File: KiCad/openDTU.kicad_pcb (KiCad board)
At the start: 2 copper layers, 42 x 46.7 mm, 26 parts, among them J1 USB_C_Receptacle_USB2.0, J2 Conn_Coaxial, U3 ESP32-WROOM-32, U4 nRF24L01P, U5 NCP1117-3.3_SOT223, Y1 Crystal

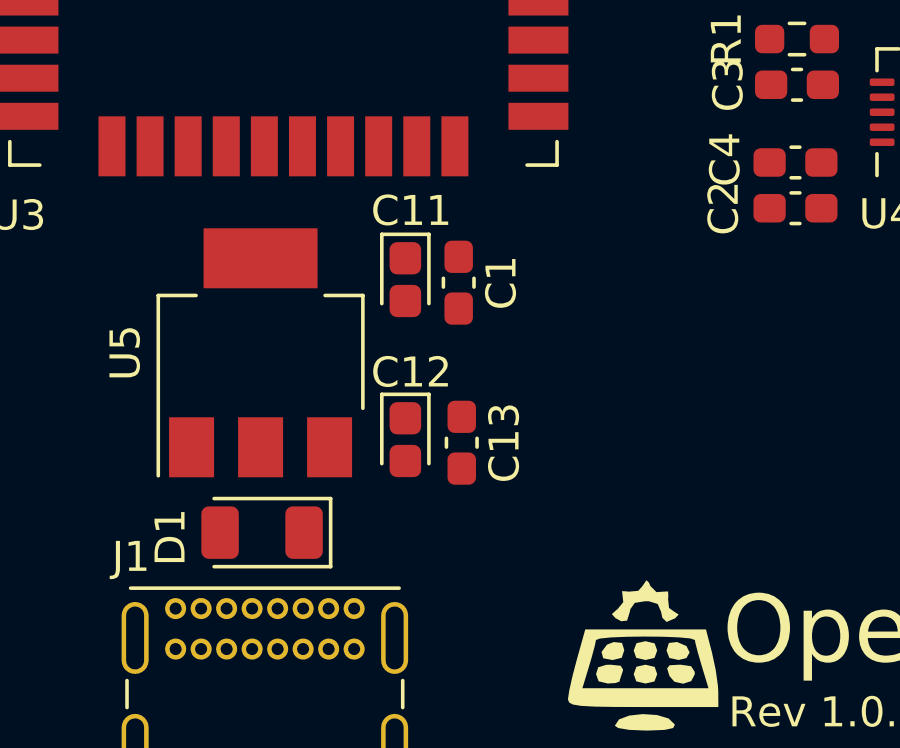
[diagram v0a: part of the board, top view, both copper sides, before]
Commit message: adding 3D Model for USB-C connector
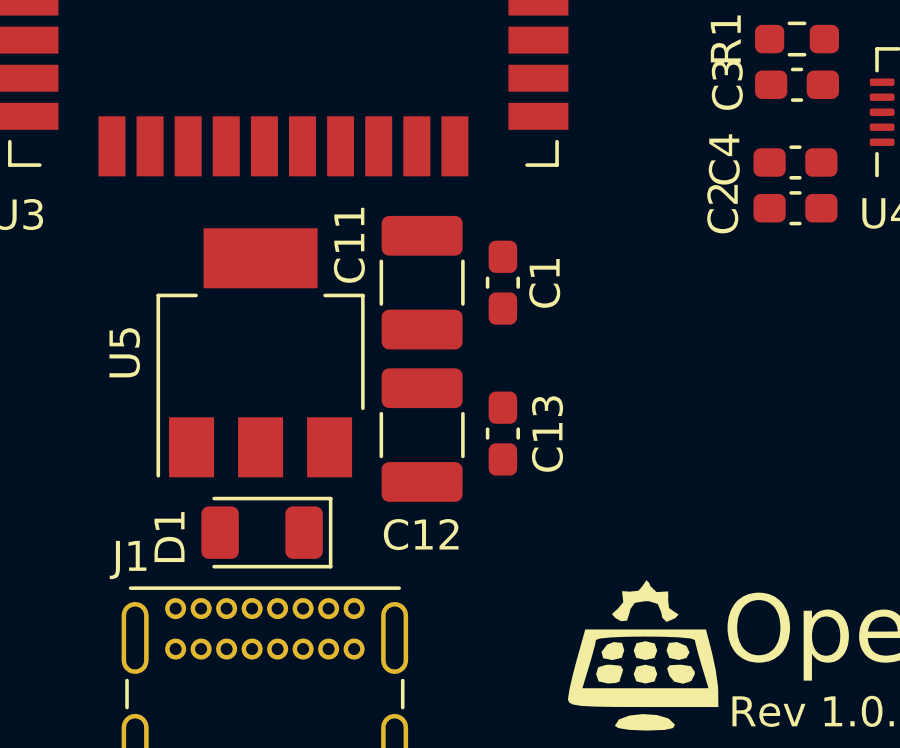
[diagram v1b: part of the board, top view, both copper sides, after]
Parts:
- C11, C12: footprint Capacitor_Tantalum_SMD:CP_EIA-1608-10_AVX-L -> Capacitor_SMD:C_1210_3225Metric_Pad1.33x2.70mm_HandSolder
- moved C1 1.47 mm to (143.5, 100.2)
- moved C13 1.41 mm to (143.5, 105.2), turned to 90 degrees
- moved C12 0.58 mm to (140.8, 105.3), turned to 90 degrees
- moved C11 0.57 mm to (140.8, 100.2)

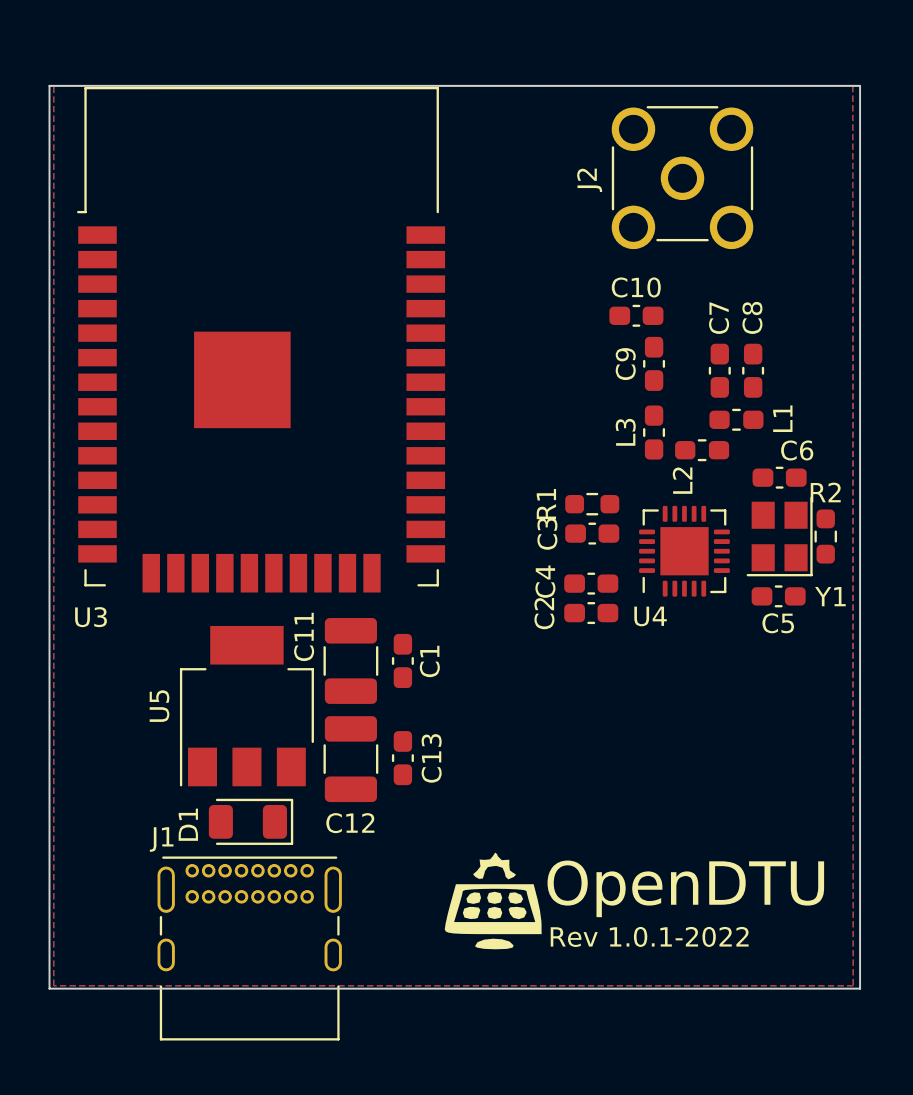
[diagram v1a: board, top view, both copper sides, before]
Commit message: adding microSD socket and reset switch to schematic
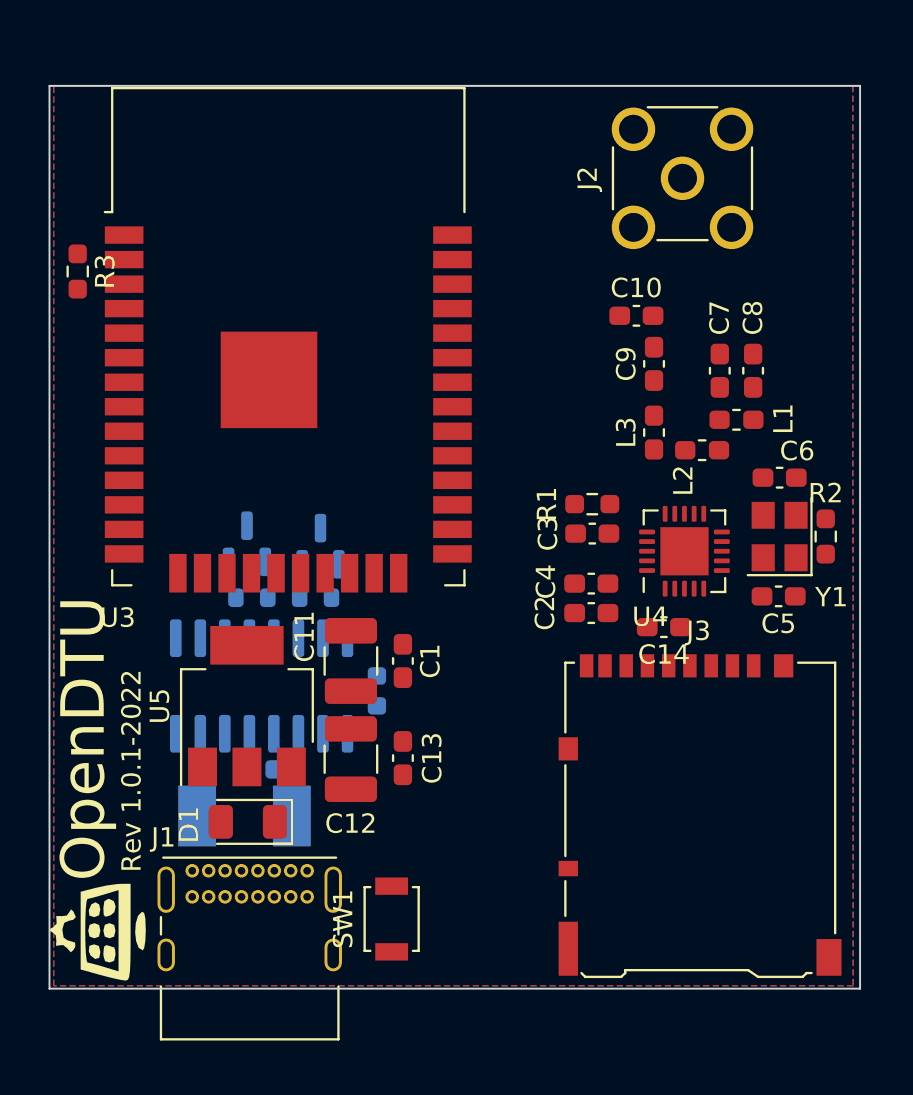
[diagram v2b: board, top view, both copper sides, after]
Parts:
- added C14: 100nF, Capacitor_SMD:C_0603_1608Metric_Pad1.08x0.95mm_HandSolder, F.Cu at (157.0, 98.4)
- added C15: 100n, Capacitor_SMD:C_0603_1608Metric, B.Cu at (136.0, 105.8)
- added C16: 100n, Capacitor_SMD:C_0603_1608Metric, B.Cu at (142.1, 101.7)
- added F1: F5, Fuse:Fuse_Littelfuse-NANO2-451_453, B.Cu at (135.3, 108.2)
- added J3: Micro_SD_Card, Connector_Card:microSD_HC_Hirose_DM3AT-SF-PEJM5, F.Cu at (158.8, 108.2)
- added Q1: BC817, Package_TO_SOT_SMD:SOT-23, B.Cu at (135.4, 94.1)
- added Q2: BC817, Package_TO_SOT_SMD:SOT-23, B.Cu at (139.2, 94.2)
- added R3: 10k, Resistor_SMD:R_0603_1608Metric_Pad0.98x0.95mm_HandSolder, F.Cu at (126.6, 80.0)
- added R4: 10k, Resistor_SMD:R_0603_1608Metric, B.Cu at (135.6, 96.9)
- added R5: 10k, Resistor_SMD:R_0603_1608Metric, B.Cu at (138.9, 96.9)
- added SW1: SW_Push, Button_Switch_SMD:SW_SPST_B3U-1000P, F.Cu at (142.9, 113.5)
- added U1: CH340C, Package_SO:SOIC-16_3.9x9.9mm_P1.27mm, B.Cu at (136.1, 101.5)
- moved G*** 20.6 mm to (127.6, 114.2), turned to 90 degrees
- moved U3 1.38 mm to (137.5, 86.4)
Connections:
- J1 pad A4: VBUS -> Net-(J1-PadA4)
- J1 pad A6: unconnected-(J1-PadA6) -> Net-(J1-PadA6)
- J1 pad A7: unconnected-(J1-PadA7) -> Net-(J1-PadA7)
- J1 pad A9: VBUS -> Net-(J1-PadA4)
- J1 pad B4: VBUS -> Net-(J1-PadA4)
- J1 pad B6: unconnected-(J1-PadB6) -> (no net)
- J1 pad B7: unconnected-(J1-PadB7) -> (no net)
- J1 pad B9: VBUS -> Net-(J1-PadA4)
- U3 pad 3: unconnected-(U3-Pad3) -> /ESP_EN

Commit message: adding BOOT switch buttom
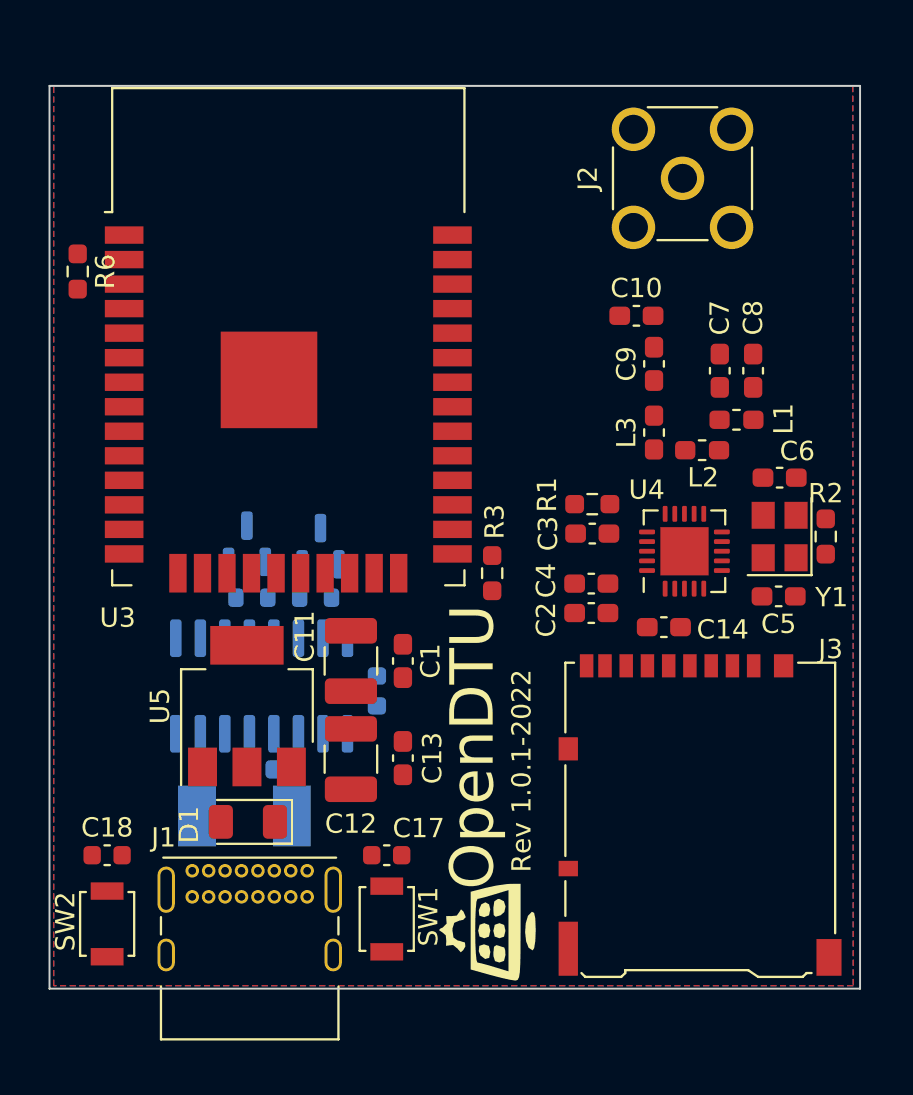
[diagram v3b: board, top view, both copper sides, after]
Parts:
- added C17: 1µ, Capacitor_SMD:C_0603_1608Metric, F.Cu at (142.6, 110.2)
- added C18: 1µ, Capacitor_SMD:C_0603_1608Metric, F.Cu at (128.1, 110.2)
- added R6: 10k, Resistor_SMD:R_0603_1608Metric_Pad0.98x0.95mm_HandSolder, F.Cu at (126.6, 80.0)
- added SW2: SW_Push, Button_Switch_SMD:SW_SPST_B3U-1000P, F.Cu at (128.1, 113.8)
- moved R3 26.5 mm to (148.1, 95.6), turned to 90 degrees
- moved G*** 20.2 mm to (147.8, 114.2)
- moved SW1 0.25 mm to (142.6, 113.5)
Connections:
- Q2 pad 3: /ESP_IO0/ETH_REFCLK -> /ESP.IO0
- R3 pad 2: /ESP_EN -> /ESP.IO0
- SW1 pad 2: /ESP_EN -> /ESP.IO0
- U1 pad 2: /ESP_RXD/BTN2 -> /ESP.RXD
- U1 pad 3: /ESP_TXD/BTN1 -> /ESP.TXD
- U3 pad 25: unconnected-(U3-Pad25) -> /ESP.IO0
- U3 pad 34: unconnected-(U3-Pad34) -> /ESP.RXD
- U3 pad 35: unconnected-(U3-Pad35) -> /ESP.TXD

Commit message: adding User (GPIO1) and Power LED
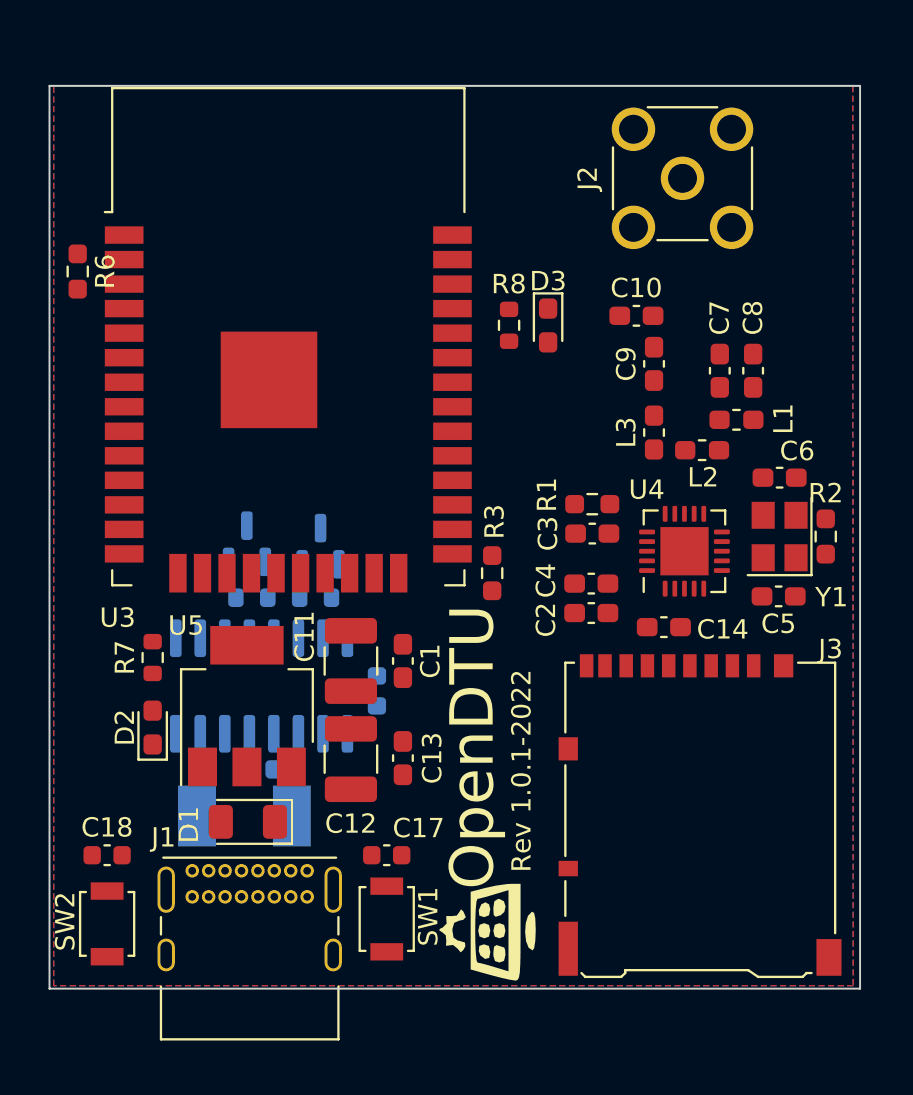
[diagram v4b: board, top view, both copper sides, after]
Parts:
- added D2: LED, LED_SMD:LED_0603_1608Metric_Pad1.05x0.95mm_HandSolder, F.Cu at (130.5, 103.6)
- added D3: LED, LED_SMD:LED_0603_1608Metric_Pad1.05x0.95mm_HandSolder, F.Cu at (151.0, 82.8)
- added R7: 10k, Resistor_SMD:R_0603_1608Metric, F.Cu at (130.5, 100.0)
- added R8: 10k, Resistor_SMD:R_0603_1608Metric, F.Cu at (149.0, 82.8)

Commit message: reduce the board size and beautify the placement
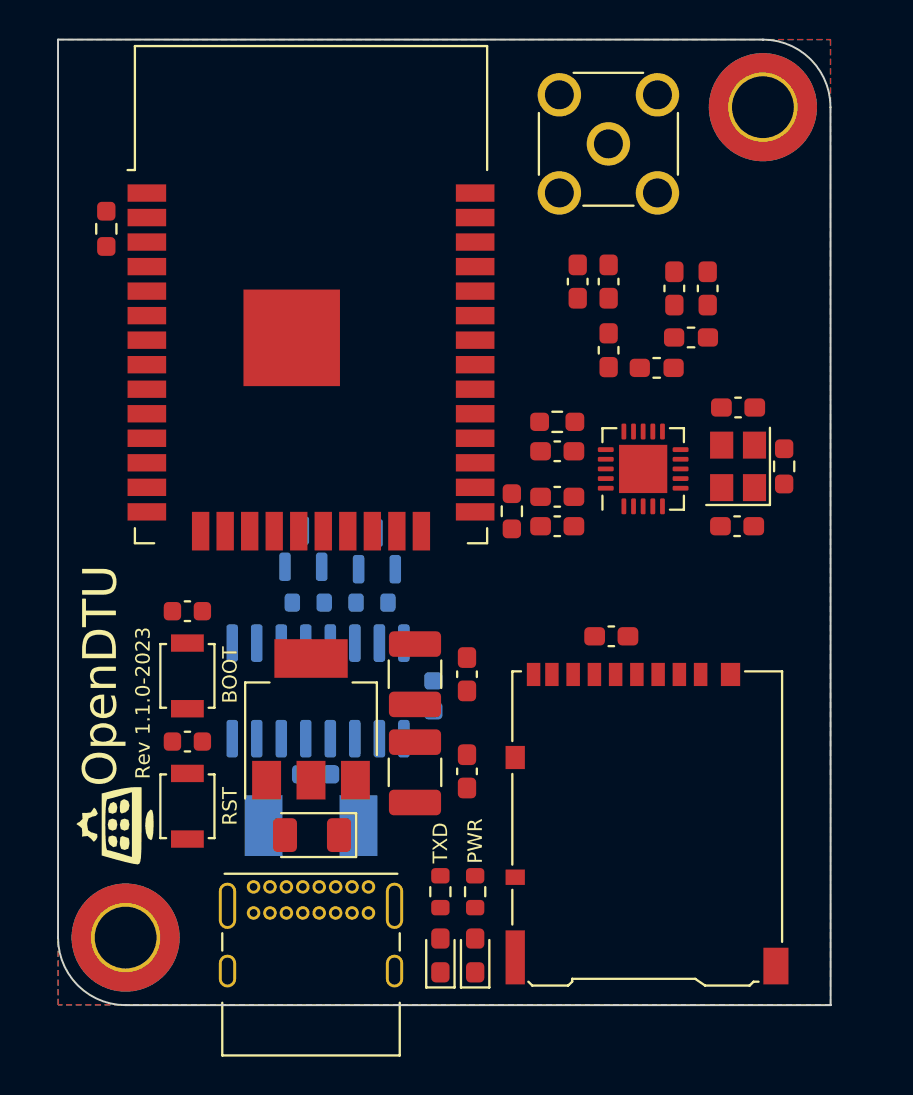
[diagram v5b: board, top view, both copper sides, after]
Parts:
- removed the G*** at (147.8, 114.2)
- added G***: LOGO, LOGO, F.Cu at (128.5, 108.7)
- added REF**: MountingHole_3.2mm_M3_DIN965_Pad_TopBottom, MountingHole:MountingHole_3.2mm_M3_DIN965_Pad_TopBottom, F.Cu at (162.1, 71.5)
- added REF**: MountingHole_3.2mm_M3_DIN965_Pad_TopBottom, MountingHole:MountingHole_3.2mm_M3_DIN965_Pad_TopBottom, F.Cu at (129.1, 114.5)
- moved D3 33.1 mm to (145.4, 115.4), turned to 90 degrees
- moved R8 29.5 mm to (145.4, 112.1)
- moved R7 20.6 mm to (147.2, 112.1)
- moved D2 20.4 mm to (147.2, 115.4)
- moved C17 16.3 mm to (132.3, 97.6), turned to 0 degrees
- moved SW1 16.3 mm to (132.3, 101.0)
- moved SW2 7.38 mm to (132.3, 107.7)
- moved C18 7.21 mm to (132.3, 104.3)
- moved C7 4.87 mm to (157.5, 80.9)
- moved L1 4.87 mm to (158.4, 83.4)
- moved L2 4.87 mm to (156.6, 85.0)
- moved C8 4.87 mm to (159.2, 80.9)
- moved C9 4.87 mm to (154.1, 80.5)
- moved L3 4.87 mm to (154.1, 84.1)
- moved C2 4.83 mm to (151.4, 93.2)
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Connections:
- net /ESP.~{CSN} renamed /ESP.~{CS}
- J3 pad 2: unconnected-(J3-Pad2) -> /ESP.~{CS}_SD
- J3 pad 3: unconnected-(J3-Pad3) -> /ESP.MOSI_SD
- J3 pad 5: unconnected-(J3-Pad5) -> /ESP.SCK_SD
- J3 pad 7: unconnected-(J3-Pad7) -> /ESP.MISO_SD
- U3 pad 13: unconnected-(U3-Pad13) -> /ESP.SCK_SD
- U3 pad 14: unconnected-(U3-Pad14) -> /ESP.MISO_SD
- U3 pad 16: unconnected-(U3-Pad16) -> /ESP.MOSI_SD
- U3 pad 23: unconnected-(U3-Pad23) -> /ESP.~{CS}_SD
- U3 pad 33: unconnected-(U3-Pad33) -> /ESP.SDA
- U3 pad 36: unconnected-(U3-Pad36) -> /ESP.SCL
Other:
- board size 42 x 46.7 mm -> 40 x 50 mm
- board text added: "BOOT"
- board text added: "PWR"
- board text added: "RST"
- board text added: "Rev 1.1.0-2023"
- board text added: "TXD"
- board text removed: "Rev 1.0.1-2022"

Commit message: routing first parts
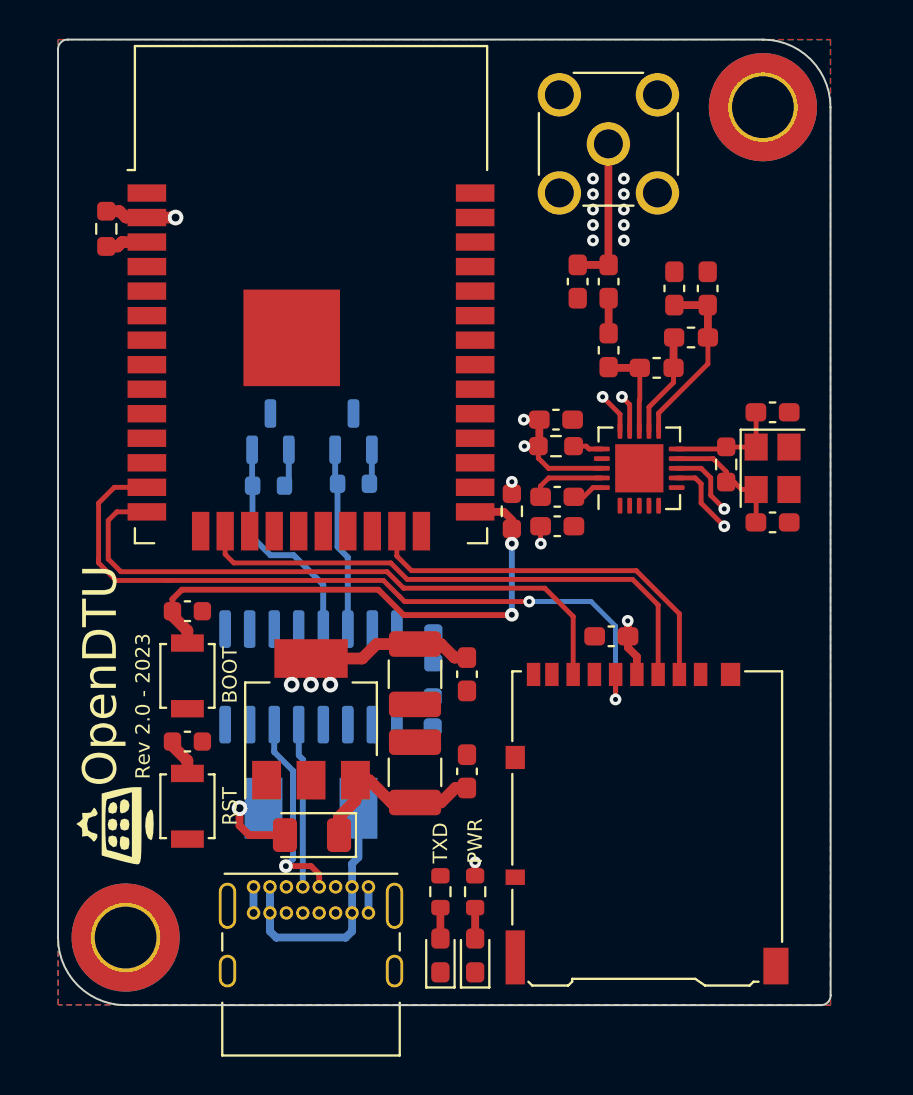
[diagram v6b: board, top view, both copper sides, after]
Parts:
- moved C15 6.87 mm to (145.0, 102.8), turned to 90 degrees
- moved R4 6.39 mm to (136.5, 91.1), turned to 0 degrees
- moved Q2 6.31 mm to (140.9, 88.3)
- moved Q1 6.30 mm to (136.6, 88.3)
- moved R5 6.23 mm to (140.9, 91.0)
- moved R2 3.00 mm to (160.2, 90.0)
- moved C16 2.48 mm to (145.0, 99.5)
- moved C5 1.85 mm to (162.6, 93.0), turned to 0 degrees
- moved C6 1.80 mm to (162.6, 87.3), turned to 0 degrees
- moved Y1 1.79 mm to (162.6, 90.2), turned to -90 degrees
- moved C3 1.64 mm to (151.4, 87.7)
- moved R1 1.26 mm to (151.4, 89.1)
- moved F1 0.90 mm to (138.7, 107.8)
- moved U1 0.81 mm to (138.7, 101.0)
- moved U4 0.20 mm to (155.7, 90.2)
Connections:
- Y1 pad 1: Net-(C5-Pad1) -> Net-(C6-Pad1)
- Y1 pad 2: Net-(C6-Pad1) -> Net-(C5-Pad1)
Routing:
- net /ESP.SCK_SD: track 0.00 -> 39.2 mm, vias 0 -> 2
- net +3.3V: track 0.00 -> 36.9 mm, vias 0 -> 12
- net /ESP.MISO_SD: track 0.00 -> 32.5 mm
- net /ESP.MOSI_SD: track 0.00 -> 28.3 mm
- net /ESP.IO0: track 0.00 -> 27.9 mm, vias 0 -> 2
- net /ESP.~{CS}_SD: track 0.00 -> 20.3 mm
- net Net-(F1-Pad1): track 0.00 -> 13.3 mm
- net Net-(Q1-Pad2): track 0.00 -> 11.5 mm
- net Net-(J1-PadA7): track 0.00 -> 10.4 mm, vias 0 -> 1
- net GND: track 0.00 -> 10.1 mm, vias 0 -> 12
- net +5V: track 0.00 -> 9.76 mm
- net Net-(Q2-Pad2): track 0.00 -> 9.56 mm
- net Net-(C7-Pad1): track 0.00 -> 9.30 mm
- net Net-(J1-PadA6): track 0.00 -> 8.49 mm
- net Net-(C10-Pad2): track 0.00 -> 7.87 mm
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- added copper zone on In1.Cu, net +3.3V
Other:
- outline, holes or cut-outs redrawn
- copper layers 2 -> 4
- board text added: "Rev 2.0 - 2023"
- board text removed: "Rev 1.1.0-2023"
